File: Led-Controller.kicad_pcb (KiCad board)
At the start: 2 copper layers, 64.8 x 49.8 mm, 42 parts, among them J1 Barrel_Jack_Switch_Pin3Ring, J2 Screw_Terminal_01x06, Q1 PMOS, Q2 PMOS, Q3 PMOS, Q4 PMOS, Q5 PMOS, U1 1ED44175N01BXTSA1, U2 1ED44175N01BXTSA1, U3 1ED44175N01BXTSA1, U4 1ED44175N01BXTSA1, U5 1ED44175N01BXTSA1, U6 ESP32-WROOM-32E, U7 AMS1117-3.3, U8 AMS1117-5.0

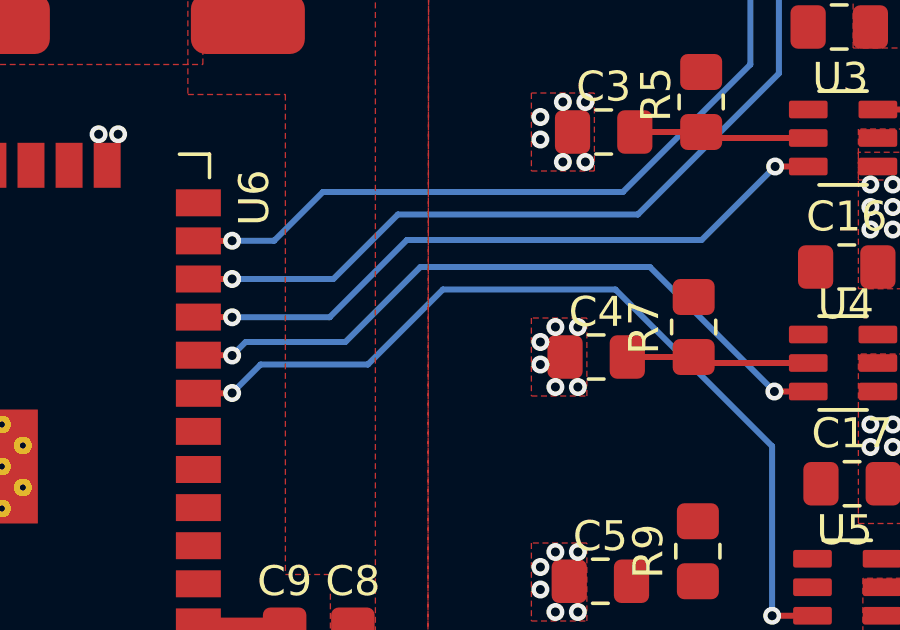
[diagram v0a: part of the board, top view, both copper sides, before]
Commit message: Fixed: Pin assignment
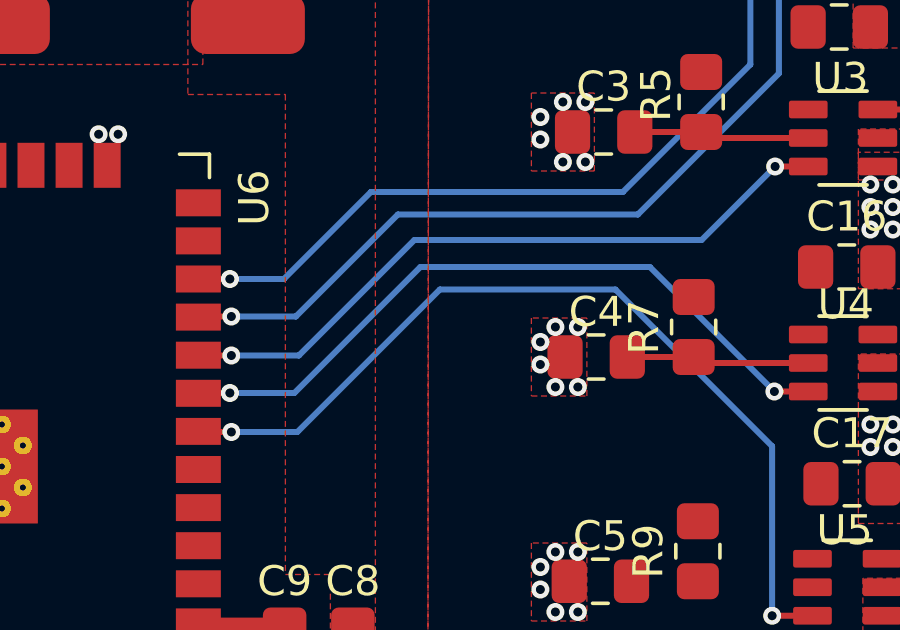
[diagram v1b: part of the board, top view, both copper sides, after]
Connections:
- U6 pad 10: /IN4 -> /IN3
- U6 pad 11: /IN3 -> /IN2
- U6 pad 12: /IN2 -> /IN1
- U6 pad 13: /IN1 -> unconnected-(U6-IO14-Pad13)
- U6 pad 8: unconnected-(U6-IO32-Pad8) -> /IN5
- U6 pad 9: /IN5 -> /IN4
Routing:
- net /IN5: track 29.7 -> 30.3 mm
- net /IN3: track 22.4 -> 22.9 mm
- net /IN1: track 34.1 -> 34.7 mm
- net /IN2: track 27.9 -> 28.4 mm
- net /IN4: track 23.3 -> 23.8 mm

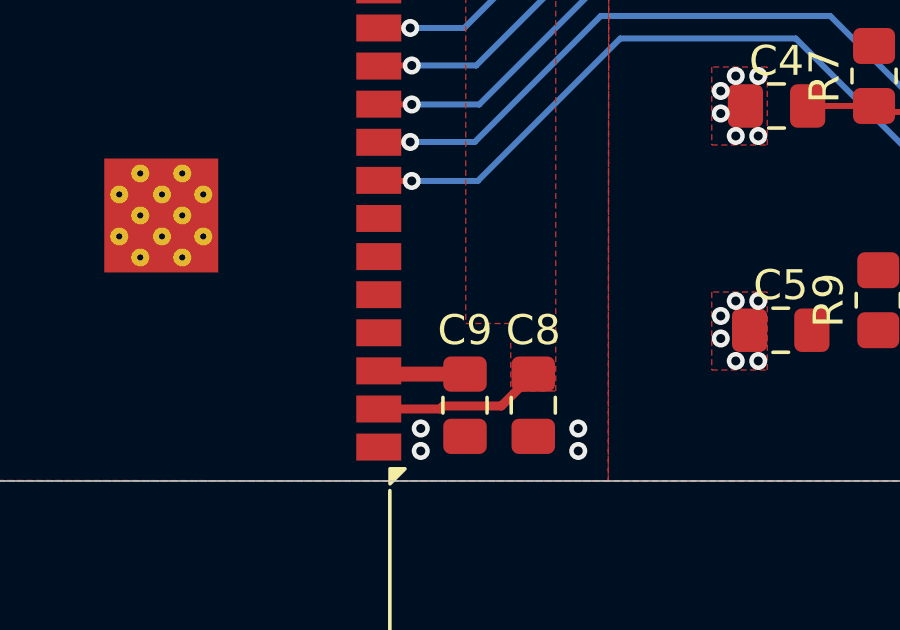
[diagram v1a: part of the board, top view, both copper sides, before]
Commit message: Added: Pull up resistor for EN pin
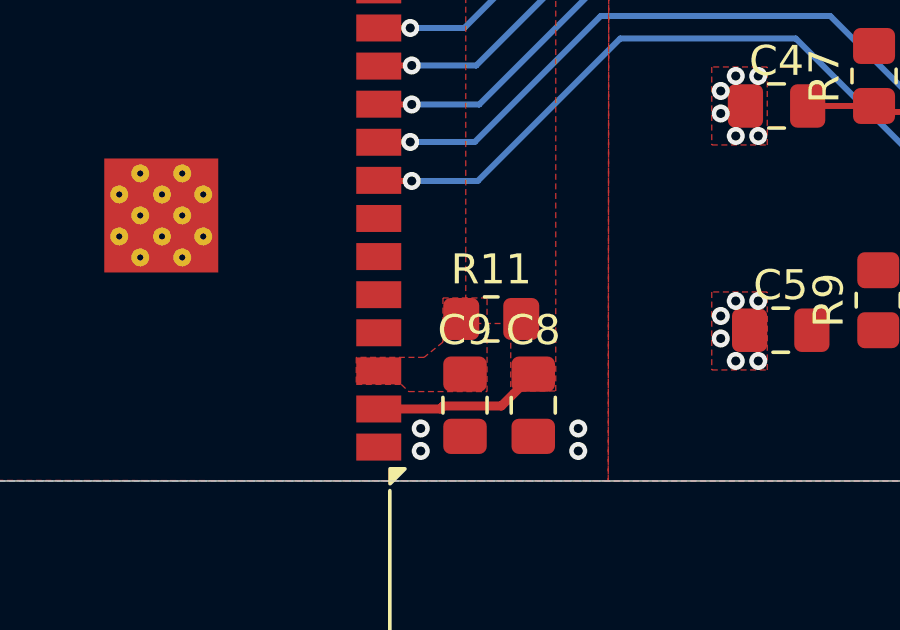
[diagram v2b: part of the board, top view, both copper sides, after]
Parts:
- added R11: 10k, Resistor_SMD:R_0805_2012Metric_Pad1.20x1.40mm_HandSolder, F.Cu at (95.6, 132.3)
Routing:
- net Net-(U6-EN): track 2.92 -> 0.33 mm
- added copper zone on F.Cu, net Net-(U6-EN)
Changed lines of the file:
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@@
 		)
 	)
+	(footprint "Resistor_SMD:R_0805_2012Metric_Pad1.20x1.40mm_HandSolder"
+		(layer "F.Cu")
+		(at 95.6 132.35)
+		(descr "Resistor SMD 0805 (2012 Metric), square (rectangular) end terminal, IPC_7351 nominal with elongated pad for handsoldering. (Body size source: IPC-SM-782 page 72, https://www.pcb-3d.com/wordpress/wp-content/uploads/ipc-sm-782a_amendment_1_and_2.pdf), generated with kicad-footprint-generator")
+		(tags "resistor handsolder")
+		(property "Reference" "R11"
+			(at 0 -1.65 0)
+			(layer "F.SilkS")
+			(effects
+				(font
+					(size 1 1)
+					(thickness 0.15)
+				)
+			)
+		)
+		(property "Value" "10k"
+			(at 0 1.65 0)
+			(layer "F.Fab")
+			(effects
+				(font
+					(size 1 1)
+					(thickness 0.15)
+				)
+			)
+		)
+		(property "Footprint" "Resistor_SMD:R_0805_2012Metric_Pad1.20x1.40mm_HandSolder"
+			(at 0 0 0)
+			(unlocked yes)
+			(layer "F.Fab")
+			(hide yes)
+			(effects
+				(font
+					(size 1.27 1.27)
+					(thickness 0.15)
+				)
+			)
+		)
+		(property "Datasheet" ""
+			(at 0 0 0)
+			(unlocked yes)
+			(layer "F.Fab")
+			(hide yes)
+			(effects
+				(font
+					(size 1.27 1.27)
+					(thickness 0.15)
+				)
+			)
+		)
+		(property "Description" "Resistor"
+			(at 0 0 0)
+			(unlocked yes)
+			(layer "F.Fab")
+			(hide yes)
+			(effects
+				(font
+					(size 1.27 1.27)
+					(thickness 0.15)
+				)
+			)
+		)
+		(property ki_fp_filters "R_*")
+		(sheetname "Root")
+		(sheetfile "Led-Controller.kicad_sch")
+		(attr smd)
+		(fp_line
+			(start -0.227064 -0.735)
+			(end 0.227064 -0.735)
+			(stroke
+				(width 0.12)
+				(type solid)
+			)
+			(layer "F.SilkS")
+		)
+		(fp_line
+			(start -0.227064 0.735)
+			(end 0.227064 0.735)
+			(stroke
+				(width 0.12)
+				(type solid)
+			)
+			(layer "F.SilkS")
+		)
+		(fp_line
+			(start -1.85 -0.95)
+			(end 1.85 -0.95)
+			(stroke
+				(width 0.05)
+				(type solid)
+			)
+			(layer "F.CrtYd")
+		)
+		(fp_line
+			(start -1.85 0.95)
+			(end -1.85 -0.95)
+			(stroke
+				(width 0.05)
+				(type solid)
+			)
+			(layer "F.CrtYd")
+		)
+		(fp_line
+			(start 1.85 -0.95)
+			(end 1.85 0.95)
+			(stroke
+				(width 0.05)
+				(type solid)
+			)
+			(layer "F.CrtYd")
+		)
+		(fp_line
+			(start 1.85 0.95)
+			(end -1.85 0.95)
+			(stroke
+				(width 0.05)
+				(type solid)
+			)
+			(layer "F.CrtYd")
+		)
+		(fp_line
+			(start -1 -0.625)
+			(end 1 -0.625)
+			(stroke
+				(width 0.1)
+				(type solid)
+			)
+			(layer "F.Fab")
+		)
+		(fp_line
+			(start -1 0.625)
+			(end -1 -0.625)
+			(stroke
+				(width 0.1)
+				(type solid)
+			)
+			(layer "F.Fab")
+		)
+		(fp_line
+			(start 1 -0.625)
+			(end 1 0.625)
+			(stroke
+				(width 0.1)
+				(type solid)
+			)
+			(layer "F.Fab")
+		)
+		(fp_line
+			(start 1 0.625)
+			(end -1 0.625)
+			(stroke
+				(width 0.1)
+				(type solid)
+			)
+			(layer "F.Fab")
+		)
+		(fp_text user "${REFERENCE}"
+			(at 0 0 0)
+			(layer "F.Fab")
+			(effects
+				(font
+					(size 0.5 0.5)
+					(thickness 0.08)
+				)
+			)
+		)
+		(pad "1" smd roundrect
+			(at -1 0)
+			(size 1.2 1.4)
+			(layers "F.Cu" "F.Paste" "F.Mask")
+			(roundrect_rratio 0.208333)
+			(net 9 "Net-(U6-EN)")
+			(pintype "passive")
+		)
+		(pad "2" smd roundrect
+			(at 1 0)
+			(size 1.2 1.4)
+			(layers "F.Cu" "F.Paste" "F.Mask")
+			(roundrect_rratio 0.208333)
+			(net 8 "+3.3V")
+			(pintype "passive")
+		)
+		(model "${KICAD8_3DMODEL_DIR}/Resistor_SMD.3dshapes/R_0805_2012Metric.wrl"
+			(offset
+				(xyz 0 0 0)
+			)
+			(scale
+				(xyz 1 1 1)
+			)
+			(rotate
+				(xyz 0 0 0)
+			)
+		)
+	)
 	(footprint "1ED44175N01BXTSA1:1ED44175N01BXTSA1"
 		(layer "F.Cu")
@@
 	)
 	(segment
-		(start 94.725 134.1875)
-		(end 91.9575 134.1875)
-		(width 0.5)
+		(start 91.9575 134.1875)
+		(end 91.85 134.08)
+		(width 0.2)
 		(layer "F.Cu")
 		(net 9)
 	)
 	(segment
-		(start 91.9575 134.1875)
-		(end 91.85 134.08)
-		(width 0.2)
+		(start 94.725 132.475)
+		(end 94.6 132.35)
+		(width 0.5)
 		(layer "F.Cu")
 		(net 9)
@@
 		(polygon
 			(pts
-				(xy 94.75 116.5) (xy 93.1 116.5) (xy 93.1 133.5) (xy 94.75 133.5)
+				(xy 94.75 116.5) (xy 93.1 116.5) (xy 93.09 131.34) (xy 94.79 131.34)
 			)
 		)
@@
 			)
 		)
+	)
+	(zone
+		(net 9)
+		(net_name "Net-(U6-EN)")
+		(layer "F.Cu")
+		(hatch edge 0.5)
+		(priority 18)
+		(connect_pads yes
+			(clearance 0)
+		)
+		(min_thickness 0.025)
+		(filled_areas_thickness no)
+		(fill yes
+			(thermal_gap 0.025)
+			(thermal_bridge_width 0.025)
+		)
+		(polygon
+			(pts
+				(xy 91.1 134.53) (xy 92.6 134.53) (xy 92.85 134.77) (xy 95.46 134.77) (xy 95.46 131.65) (xy 93.99 131.65)
+				(xy 93.99 133.12) (xy 93.36 133.63) (xy 91.1 133.63)
+			)
+		)

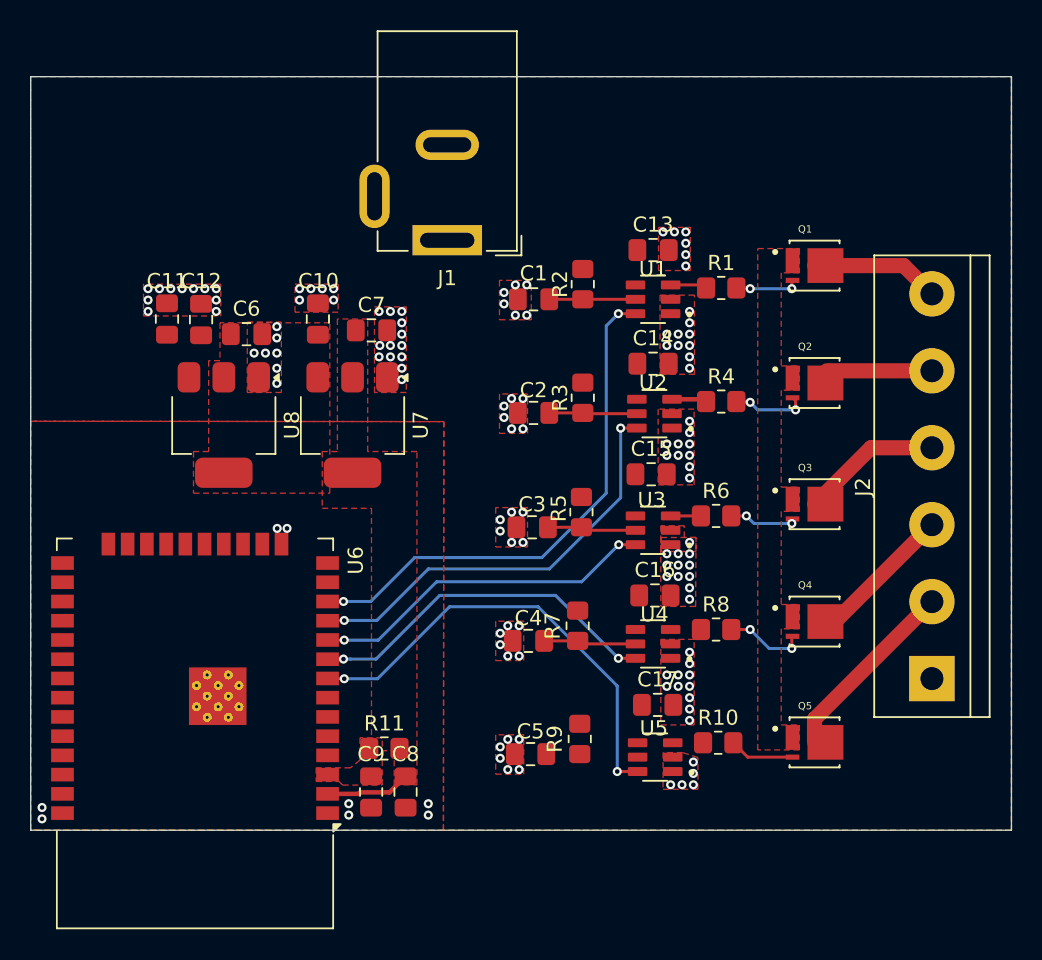
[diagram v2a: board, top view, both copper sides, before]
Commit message: Added: N channel mosfet in place of P channel mosfet
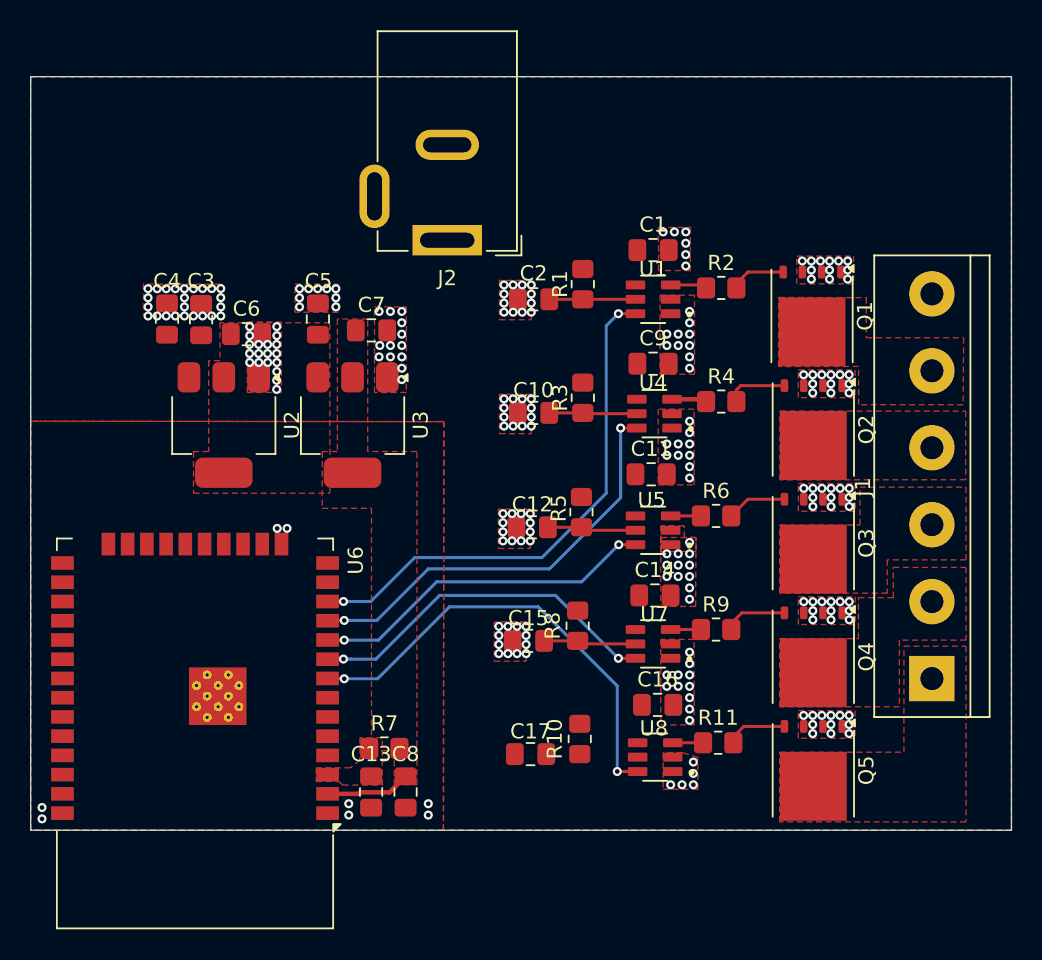
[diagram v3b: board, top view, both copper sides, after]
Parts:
- Q1, Q2, Q3, Q4, Q5: value PMOS -> CSD18540Q5B; footprint BSZ180P03:BSZ180P03 -> Package_TO_SOT_SMD:TDSON-8-1
- moved Q1 3.33 mm to (123.8, 103.8), turned to -90 degrees
- moved Q2 3.08 mm to (123.9, 111.3), turned to -90 degrees
- moved Q3 2.58 mm to (123.9, 118.8), turned to -90 degrees
- moved Q4 2.33 mm to (123.9, 126.3), turned to -90 degrees
- moved Q5 1.85 mm to (123.9, 133.8), turned to -90 degrees
- renumbered C13 to C1, C2 to C10, C15 to C11, C3 to C12, C9 to C13, C16 to C14, C4 to C15, C17 to C16, C5 to C17, C1 to C2, C12 to C3, C11 to C4, C10 to C5, C14 to C9, J2 to J1, J1 to J2, R2 to R1, R9 to R10, R10 to R11, R1 to R2, R11 to R7, R7 to R8, R8 to R9, U8 to U2, U7 to U3, U2 to U4, U3 to U5, U4 to U7, U5 to U8
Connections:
- J1 pad 1: GND -> Net-(J1-Pin_1)
- J1 pad 2: Net-(J2-Pin_2) -> Net-(J1-Pin_2)
- J1 pad 3: Net-(J2-Pin_3) -> Net-(J1-Pin_3)
- J1 pad 4: Net-(J2-Pin_4) -> Net-(J1-Pin_4)
- J1 pad 5: Net-(J2-Pin_5) -> Net-(J1-Pin_5)
- J1 pad 6: Net-(J2-Pin_6) -> VCC
- Q1 pad 1: Net-(J2-Pin_6) -> GND
- Q1 pad 2: Net-(Q1-G) -> GND
- Q1 pad 3: VCC -> GND
- Q2 pad 1: Net-(J2-Pin_5) -> GND
- Q2 pad 2: Net-(Q2-G) -> GND
- Q2 pad 3: VCC -> GND
- Q3 pad 1: Net-(J2-Pin_4) -> GND
- Q3 pad 2: Net-(Q3-G) -> GND
- Q3 pad 3: VCC -> GND
- Q4 pad 1: Net-(J2-Pin_3) -> GND
- Q4 pad 2: Net-(Q4-G) -> GND
- Q4 pad 3: VCC -> GND
- Q5 pad 1: Net-(J2-Pin_2) -> GND
- Q5 pad 2: Net-(Q5-G) -> GND
- Q5 pad 3: VCC -> GND
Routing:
- net Net-(J2-Pin_2): track 12.5 -> 0.00 mm
- net Net-(J2-Pin_3): track 10.4 -> 0.00 mm
- net Net-(J2-Pin_4): track 9.29 -> 0.00 mm
- net Net-(J2-Pin_6): track 8.52 -> 0.00 mm
- net Net-(J2-Pin_5): track 8.08 -> 0.00 mm
- net Net-(U8-OUT): track 0.00 -> 2.00 mm
- net Net-(U7-OUT): track 0.00 -> 2.00 mm
- net Net-(Q4-G): track 5.34 -> 4.20 mm, vias 2 -> 0
- net Net-(Q2-G): track 5.02 -> 4.06 mm, vias 2 -> 0
- net Net-(Q3-G): track 4.53 -> 3.97 mm, vias 2 -> 0
- net Net-(Q1-G): track 4.25 -> 3.69 mm, vias 2 -> 0
- net GND: vias 129 -> 235
- added copper zone on F.Cu, net Net-(J1-Pin_1)
- added copper zone on F.Cu, net Net-(J1-Pin_2)
- added copper zone on F.Cu, net Net-(J1-Pin_3)
- added copper zone on F.Cu, net Net-(J1-Pin_4)
- added copper zone on F.Cu, net Net-(J1-Pin_5)
